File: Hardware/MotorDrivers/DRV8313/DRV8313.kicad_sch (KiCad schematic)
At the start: 62 parts, among them CN10 PR5L4015-5P-C-F, CN11 PR5L4015-5P-C-F, CN7 PR5L4015-5P-C-F, CN8 PR5L4015-5P-C-F, CN9 PR5L4015-5P-C-F, J1 Conn_01x04_Socket, J2 Conn_01x04_Socket, J3 Conn_01x02_Socket, J4 Conn_01x03_Socket, Q1 BSS123_C427379, Q2 BSS123_C427379, U1 MS8313, U2 TLV9001IDCK, U35 PR5L5015-5P-C-H, U36 PR5L5015-5P-C-H, U37 PR5L5015-5P-C-H, U38 PR5L5015-5P-C-H, U39 PR5L5015-5P-C-H, U5 INA241A2xD, U6 INA241A2xD, U7 INA241A2xD

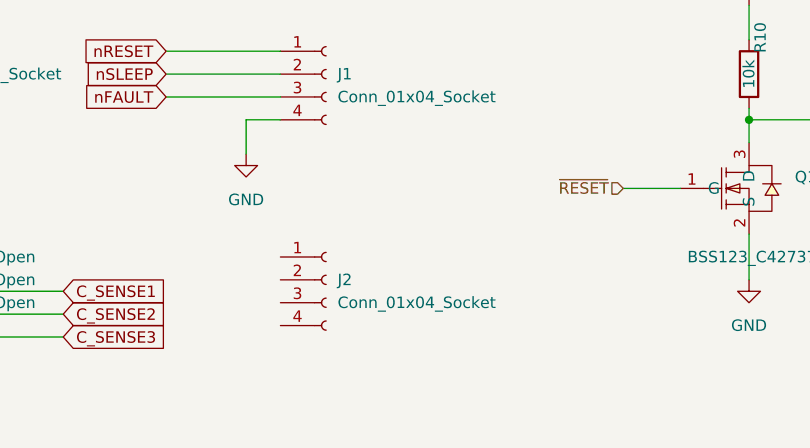
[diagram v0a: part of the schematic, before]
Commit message: DRV8313 board done component assignment
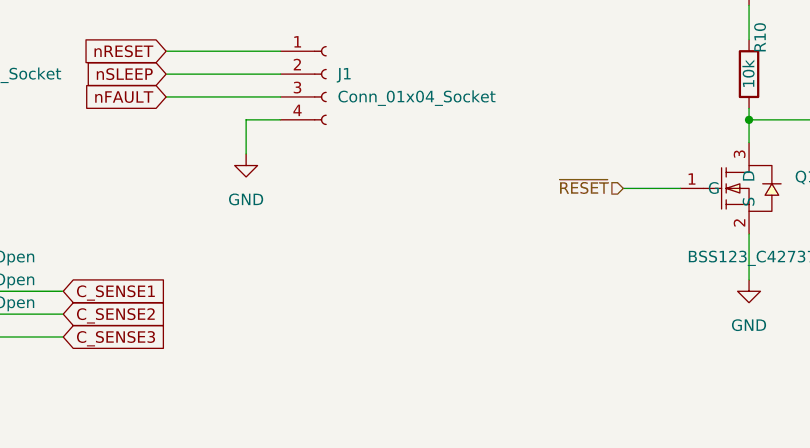
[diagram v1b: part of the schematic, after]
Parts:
- removed J2: Conn_01x04_Socket, symbol Connector:Conn_01x04_Socket
- C1, C10, C11, C12, C13, C2, C3, C4, C5, C6, C7, C8, C9, R1, R10, R2, R3, R4, R5, R9: footprint (none) -> SpaghettiLAB:C0603
- J1: footprint (none) -> Connector_PinSocket_1.27mm:PinSocket_1x04_P1.27mm_Vertical
- J3: footprint (none) -> Connector_PinSocket_1.27mm:PinSocket_1x02_P1.27mm_Vertical_SMD_Pin1Right
- J4: footprint (none) -> Connector_JST:JST_GH_SM03B-GHS-TB_1x03-1MP_P1.25mm_Horizontal
- JP1, JP10, JP11, JP2, JP3, JP4, JP5, JP6, JP7, JP8, JP9: footprint (none) -> Jumper:SolderJumper-2_P1.3mm_Open_Pad1.0x1.5mm
- R6, R7, R8: footprint (none) -> SpaghettiLAB:RES-SMD_L6.4-W3.2-R2512
- TP1, TP2, TP3: footprint (none) -> TestPoint:TestPoint_THTPad_2.5x2.5mm_Drill1.2mm
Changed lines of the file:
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@@
 			)
 		)
-		(property "Footprint" ""
+		(property "Footprint" "Jumper:SolderJumper-2_P1.3mm_Open_Pad1.0x1.5mm"
 			(at 209.55 261.62 0)
 			(hide yes)
@@
 			)
 		)
-		(property "Footprint" ""
+		(property "Footprint" "SpaghettiLAB:C0603"
 			(at 111.76 141.9352 0)
 			(hide yes)
@@
 			)
 		)
-		(property "Footprint" ""
+		(property "Footprint" "SpaghettiLAB:C0603"
 			(at 45.212 167.64 90)
 			(hide yes)
@@
 			)
 		)
-		(property "Footprint" ""
+		(property "Footprint" "SpaghettiLAB:C0603"
 			(at 177.8 140.6652 0)
 			(hide yes)
@@
 			)
 		)
-		(property "Footprint" ""
+		(property "Footprint" "TestPoint:TestPoint_THTPad_2.5x2.5mm_Drill1.2mm"
 			(at 100.33 142.24 0)
 			(hide yes)
@@
 			)
 		)
-		(property "Footprint" ""
+		(property "Footprint" "SpaghettiLAB:C0603"
 			(at 96.52 63.8048 0)
 			(hide yes)
@@
 			)
 		)
-		(property "Footprint" ""
+		(property "Footprint" "SpaghettiLAB:C0603"
 			(at 55.5752 86.36 0)
 			(hide yes)
@@
 			)
 		)
-		(property "Footprint" ""
+		(property "Footprint" "SpaghettiLAB:C0603"
 			(at 177.8 89.408 90)
 			(hide yes)
@@
 			)
 		)
-		(property "Footprint" ""
+		(property "Footprint" "Jumper:SolderJumper-2_P1.3mm_Open_Pad1.0x1.5mm"
 			(at 173.99 264.16 0)
 			(hide yes)
@@
 			)
 		)
-		(property "Footprint" ""
+		(property "Footprint" "SpaghettiLAB:RES-SMD_L6.4-W3.2-R2512"
 			(at 159.512 149.86 90)
 			(hide yes)
@@
 			)
 		)
-		(property "Footprint" ""
+		(property "Footprint" "SpaghettiLAB:C0603"
 			(at 181.3052 172.72 0)
 			(hide yes)
@@
 			)
 		)
-		(property "Footprint" ""
+		(property "Footprint" "SpaghettiLAB:C0603"
 			(at 177.8 84.328 90)
 			(hide yes)
@@
 			)
 		)
-		(property "Footprint" ""
+		(property "Footprint" "Jumper:SolderJumper-2_P1.3mm_Open_Pad1.0x1.5mm"
 			(at 48.26 265.43 0)
 			(hide yes)
@@
 			)
 		)
-		(property "Footprint" ""
+		(property "Footprint" "SpaghettiLAB:C0603"
 			(at 115.2652 173.99 0)
 			(hide yes)
@@
 			)
 		)
-		(property "Footprint" ""
+		(property "Footprint" "Jumper:SolderJumper-2_P1.3mm_Open_Pad1.0x1.5mm"
 			(at 48.26 267.97 0)
 			(hide yes)
@@
 			)
 		)
-		(property "Footprint" ""
+		(property "Footprint" "SpaghettiLAB:C0603"
 			(at 250.19 140.6652 0)
 			(hide yes)
@@
 			)
 		)
-		(property "Footprint" ""
+		(property "Footprint" "Jumper:SolderJumper-2_P1.3mm_Open_Pad1.0x1.5mm"
 			(at 173.99 274.32 0)
 			(hide yes)
@@
 			)
 		)
-		(property "Footprint" ""
+		(property "Footprint" "SpaghettiLAB:C0603"
 			(at 253.6952 171.45 0)
 			(hide yes)
@@
 			)
 		)
-		(property "Footprint" ""
+		(property "Footprint" "TestPoint:TestPoint_THTPad_2.5x2.5mm_Drill1.2mm"
 			(at 238.76 140.97 0)
 			(hide yes)
@@
 			)
 		)
-		(property "Footprint" ""
+		(property "Footprint" "Jumper:SolderJumper-2_P1.3mm_Open_Pad1.0x1.5mm"
 			(at 173.99 279.4 0)
 			(hide yes)
@@
 			)
 		)
-		(property "Footprint" ""
+		(property "Footprint" "SpaghettiLAB:C0603"
 			(at 121.92 56.1848 0)
 			(hide yes)
@@
 			)
 		)
-		(property "Footprint" ""
+		(property "Footprint" "SpaghettiLAB:C0603"
 			(at 193.3448 93.98 0)
 			(hide yes)
@@
 			)
 		)
-		(property "Footprint" ""
+		(property "Footprint" "SpaghettiLAB:C0603"
 			(at 104.14 83.5152 0)
 			(hide yes)
@@
 			)
 		)
-		(property "Footprint" ""
+		(property "Footprint" "Connector_PinSocket_1.27mm:PinSocket_1x04_P1.27mm_Vertical"
 			(at 90.17 241.3 0)
 			(hide yes)
@@
 			)
 		)
-		(property "Footprint" ""
+		(property "Footprint" "Connector_JST:JST_GH_SM03B-GHS-TB_1x03-1MP_P1.25mm_Horizontal"
 			(at 224.79 275.59 0)
 			(hide yes)
@@
 			)
 		)
-		(property "Footprint" ""
+		(property "Footprint" "SpaghettiLAB:RES-SMD_L6.4-W3.2-R2512"
 			(at 231.902 149.86 90)
 			(hide yes)
@@
 			)
 		)
-		(property "Footprint" ""
+		(property "Footprint" "SpaghettiLAB:C0603"
 			(at 60.6552 175.26 0)
 			(hide yes)
@@
 			)
 		)
-		(property "Footprint" ""
+		(property "Footprint" "Jumper:SolderJumper-2_P1.3mm_Open_Pad1.0x1.5mm"
 			(at 256.54 261.62 0)
 			(hide yes)
@@
 			)
 		)
-		(property "Footprint" ""
+		(property "Footprint" "Jumper:SolderJumper-2_P1.3mm_Open_Pad1.0x1.5mm"
 			(at 173.99 269.24 0)
 			(hide yes)
@@
 			)
 		)
-		(property "Footprint" ""
+		(property "Footprint" "SpaghettiLAB:C0603"
 			(at 177.8 86.868 90)
 			(hide yes)
@@
 			)
 		)
-		(property "Footprint" ""
+		(property "Footprint" "Jumper:SolderJumper-2_P1.3mm_Open_Pad1.0x1.5mm"
 			(at 54.61 167.64 0)
 			(hide yes)
@@
 			)
 		)
-		(property "Footprint" ""
+		(property "Footprint" "SpaghettiLAB:C0603"
 			(at 138.938 241.3 90)
 			(hide yes)
@@
 			)
 		)
-		(property "Footprint" ""
+		(property "Footprint" "SpaghettiLAB:C0603"
 			(at 45.212 154.94 90)
 			(hide yes)
@@
 			)
 		)
-		(property "Footprint" ""
+		(property "Footprint" "Jumper:SolderJumper-2_P1.3mm_Open_Pad1.0x1.5mm"
 			(at 96.52 198.12 0)
 			(hide yes)
@@
 			)
 		)
-		(property "Footprint" ""
+		(property "Footprint" "SpaghettiLAB:C0603"
 			(at 173.99 69.088 90)
 			(hide yes)
@@
 	)
 	(symbol
-		(lib_id "Connector:Conn_01x04_Socket")
-		(at 90.17 264.16 0)
-		(unit 1)
-		(body_style 1)
-		(exclude_from_sim no)
-		(in_bom yes)
-		(on_board yes)
-		(in_pos_files yes)
-		(dnp no)
-		(fields_autoplaced yes)
-		(property "Reference" "J2"
-			(at 91.44 264.1599 0)
-			(show_name no)
-			(do_not_autoplace no)
-			(effects
-				(font
-					(size 1.27 1.27)
-				)
-				(justify left)
-			)
-		)
-		(property "Value" "Conn_01x04_Socket"
-			(at 91.44 266.6999 0)
-			(show_name no)
-			(do_not_autoplace no)
-			(effects
-				(font
-					(size 1.27 1.27)
-				)
-				(justify left)
-			)
-		)
-		(property "Footprint" ""
-			(at 90.17 264.16 0)
-			(hide yes)
-			(show_name no)
-			(do_not_autoplace no)
-			(effects
-				(font
-					(size 1.27 1.27)
-				)
-			)
-		)
-		(property "Datasheet" ""
-			(at 90.17 264.16 0)
-			(hide yes)
-			(show_name no)
-			(do_not_autoplace no)
-			(effects
-				(font
-					(size 1.27 1.27)
-				)
-			)
-		)
-		(property "Description" "Generic connector, single row, 01x04, script generated"
-			(at 90.17 264.16 0)
-			(hide yes)
-			(show_name no)
-			(do_not_autoplace no)
-			(effects
-				(font
-					(size 1.27 1.27)
-				)
-			)
-		)
-		(pin "2"
-		)
-		(pin "3"
-		)
-		(pin "4"
-		)
-		(pin "1"
-		)
-		(instances
-			(project "DRV8313"
-				(path "/e5d6139c-9aca-456b-814f-0648ddbeda45"
-					(reference "J2")
-					(unit 1)
-				)
-			)
-		)
-	)
-	(symbol
 		(lib_id "power:GND")
 		(at 143.51 199.39 0)
@@
 			)
 		)
-		(property "Footprint" ""
+		(property "Footprint" "SpaghettiLAB:C0603"
 			(at 118.11 61.2648 0)
 			(hide yes)
@@
 			)
 		)
-		(property "Footprint" ""
+		(property "Footprint" "TestPoint:TestPoint_THTPad_2.5x2.5mm_Drill1.2mm"
 			(at 166.37 140.97 0)
 			(hide yes)
@@
 			)
 		)
-		(property "Footprint" ""
+		(property "Footprint" "Jumper:SolderJumper-2_P1.3mm_Open_Pad1.0x1.5mm"
 			(at 48.26 270.51 0)
 			(hide yes)
@@
 			)
 		)
-		(property "Footprint" ""
+		(property "Footprint" "SpaghettiLAB:RES-SMD_L6.4-W3.2-R2512"
 			(at 93.472 151.13 90)
 			(hide yes)
@@
 			)
 		)
-		(property "Footprint" ""
+		(property "Footprint" "Connector_PinSocket_1.27mm:PinSocket_1x02_P1.27mm_Vertical_SMD_Pin1Right"
 			(at 41.91 238.76 0)
 			(hide yes)

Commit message: Added test point smaller for out current sense
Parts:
- TP1, TP2, TP3: footprint TestPoint:TestPoint_THTPad_2.5x2.5mm_Drill1.2mm -> TestPoint:TestPoint_THTPad_1.0x1.0mm_Drill0.5mm
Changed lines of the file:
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@@
 			)
 		)
-		(property "Footprint" "TestPoint:TestPoint_THTPad_2.5x2.5mm_Drill1.2mm"
+		(property "Footprint" "TestPoint:TestPoint_THTPad_1.0x1.0mm_Drill0.5mm"
 			(at 100.33 142.24 0)
 			(hide yes)
@@
 			)
 		)
-		(property "Footprint" "TestPoint:TestPoint_THTPad_2.5x2.5mm_Drill1.2mm"
+		(property "Footprint" "TestPoint:TestPoint_THTPad_1.0x1.0mm_Drill0.5mm"
 			(at 238.76 140.97 0)
 			(hide yes)
@@
 			)
 		)
-		(property "Footprint" "TestPoint:TestPoint_THTPad_2.5x2.5mm_Drill1.2mm"
+		(property "Footprint" "TestPoint:TestPoint_THTPad_1.0x1.0mm_Drill0.5mm"
 			(at 166.37 140.97 0)
 			(hide yes)

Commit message: Minor fix to connectors footprint
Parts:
- J3: footprint Connector_PinSocket_1.27mm:PinSocket_1x02_P1.27mm_Vertical_SMD_Pin1Right -> Connector_PinSocket_1.27mm:PinSocket_1x03_P1.27mm_Vertical
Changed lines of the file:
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@@
 			)
 		)
-		(property "Footprint" "Connector_PinSocket_1.27mm:PinSocket_1x02_P1.27mm_Vertical_SMD_Pin1Right"
+		(property "Footprint" "Connector_PinSocket_1.27mm:PinSocket_1x03_P1.27mm_Vertical"
 			(at 41.91 238.76 0)
 			(hide yes)

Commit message: placed components
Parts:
- C4: footprint SpaghettiLAB:C0603 -> SpaghettiLAB:C1206
- J3: footprint Connector_PinSocket_1.27mm:PinSocket_1x03_P1.27mm_Vertical -> Connector_PinSocket_1.27mm:PinSocket_1x02_P1.27mm_Vertical
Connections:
- net OUT1: now also J4.3 (Pin_3); no longer J4.1 (Pin_1)
- net OUT3: now also J4.1 (Pin_1); no longer J4.3 (Pin_3)
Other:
- note removed: "NEAR TO LOAD"
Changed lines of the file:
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@@
 		)
 	)
-	(text "NEAR TO LOAD"
-		(exclude_from_sim no)
-		(at 64.262 87.122 0)
-		(effects
-			(font
-				(size 1.27 1.27)
-			)
-		)
-	)
 	(text "MOTOR DRIVER\n"
 		(exclude_from_sim no)
@@
 		)
 	)
-	(global_label "nFAULT"
+	(global_label "OUT1"
 		(shape input)
-		(at 72.39 243.84 180)
+		(at 204.47 278.13 180)
 		(fields_autoplaced yes)
 		(effects
@@
 		)
 		(property "Intersheetrefs" "${INTERSHEET_REFS}"
-			(at 62.7524 243.84 0)
+			(at 196.6467 278.13 0)
 			(hide yes)
 			(show_name no)
@@
 		)
 	)
-	(global_label "OUT1"
+	(global_label "nFAULT"
 		(shape input)
-		(at 204.47 273.05 180)
+		(at 72.39 243.84 180)
 		(fields_autoplaced yes)
 		(effects
@@
 		)
 		(property "Intersheetrefs" "${INTERSHEET_REFS}"
-			(at 196.6467 273.05 0)
+			(at 62.7524 243.84 0)
 			(hide yes)
 			(show_name no)
@@
 		)
 	)
-	(global_label "OUT3"
+	(global_label "C_SENSE2"
 		(shape input)
-		(at 204.47 278.13 180)
+		(at 203.2 149.86 0)
 		(fields_autoplaced yes)
 		(effects
@@
 				(size 1.27 1.27)
 			)
-			(justify right)
+			(justify left)
 		)
 		(property "Intersheetrefs" "${INTERSHEET_REFS}"
-			(at 196.6467 278.13 0)
+			(at 215.6798 149.86 0)
 			(hide yes)
 			(show_name no)
@@
 					(size 1.27 1.27)
 				)
-				(justify right)
+				(justify left)
 			)
 		)
 	)
-	(global_label "C_SENSE2"
+	(global_label "OUT3"
 		(shape input)
-		(at 203.2 149.86 0)
+		(at 204.47 273.05 180)
 		(fields_autoplaced yes)
 		(effects
@@
 				(size 1.27 1.27)
 			)
-			(justify left)
+			(justify right)
 		)
 		(property "Intersheetrefs" "${INTERSHEET_REFS}"
-			(at 215.6798 149.86 0)
+			(at 196.6467 273.05 0)
 			(hide yes)
 			(show_name no)
@@
 					(size 1.27 1.27)
 				)
-				(justify left)
+				(justify right)
 			)
 		)
@@
 			)
 		)
-		(property "Footprint" "SpaghettiLAB:C0603"
+		(property "Footprint" "SpaghettiLAB:C1206"
 			(at 55.5752 86.36 0)
 			(hide yes)
@@
 			)
 		)
-		(property "Footprint" "Connector_PinSocket_1.27mm:PinSocket_1x03_P1.27mm_Vertical"
+		(property "Footprint" "Connector_PinSocket_1.27mm:PinSocket_1x02_P1.27mm_Vertical"
 			(at 41.91 238.76 0)
 			(hide yes)

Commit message: Started routing and fixed flex label in core rp2350
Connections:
- net +3.3V: now also C7.2, C8.2, C9.2, U5.6 (V+), U6.6 (V+), U7.6 (V+); no longer C3.2, U1.15 (V3P3OUT)
- net VCC: no longer C7.2, C8.2, C9.2, U5.6 (V+), U6.6 (V+), U7.6 (V+)
- new net V3P3: C3.2, U1.15 (V3P3OUT)
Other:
- moved on the sheet: C3
